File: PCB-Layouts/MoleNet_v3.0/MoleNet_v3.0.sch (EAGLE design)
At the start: 58 parts, among them Q3 BS250, Q4 BS170, Q5 BS250, Q6 BS170, Q7 BS250, Q8 BS170, U1 MCP1703DB, U2 ATMEGA1284p, U4 25LC080P, U5 MCP7940M, U7 BATHOLDER, X1 SMA-142-0711-821/826

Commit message: Updated schematic and board file v3.0
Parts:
- removed JP10, JP12: (no value), pinhead:PINHD-1X12
- removed R13: 4.7K, rcl:R-EU_0207/10
- added JP7: (no value), pinhead:PINHD-1X13
- added JP8: (no value), pinhead:PINHD-1X11
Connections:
- removed net PCINT23: JP12.3, U2.TOSC2/PCINT23
- removed net VSEN+: JP6.2
- net +3V3: no longer R13.2
- net ADC1: now also JP7.1; no longer R13.1
- net ADC2: now also JP7.9; no longer JP10.8
- net ADC3: now also JP7.12; no longer JP10.11
- net ADC4: now also JP7.13; no longer JP10.12
- net ADC5: now also JP7.8; no longer JP10.7
- net ADC6: now also JP7.5; no longer JP10.4
- net ADC7: now also JP7.4; no longer JP10.3
- net ADCVCC: now also JP7.11, JP7.3, JP7.7; no longer JP10.10, JP10.2, JP10.6
- net DIGVCC: now also JP8.2, JP8.5, JP8.9; no longer JP12.10, JP12.2, JP12.6
- net GND: now also JP6.2, JP7.10, JP7.2, JP7.6, JP8.1, JP8.4, JP8.8; no longer JP10.1, JP10.5, JP10.9, JP12.1, JP12.5, JP12.9
- net NSS: now also U2.TOSC2/PCINT23
- net PCINT18: now also JP8.11; no longer JP12.12
- net PCINT19: now also JP8.10; no longer JP12.11
- net PCINT20: now also JP8.7; no longer JP12.8
- net PCINT21: now also JP8.6; no longer JP12.7
- net PCINT22: now also JP8.3; no longer JP12.4

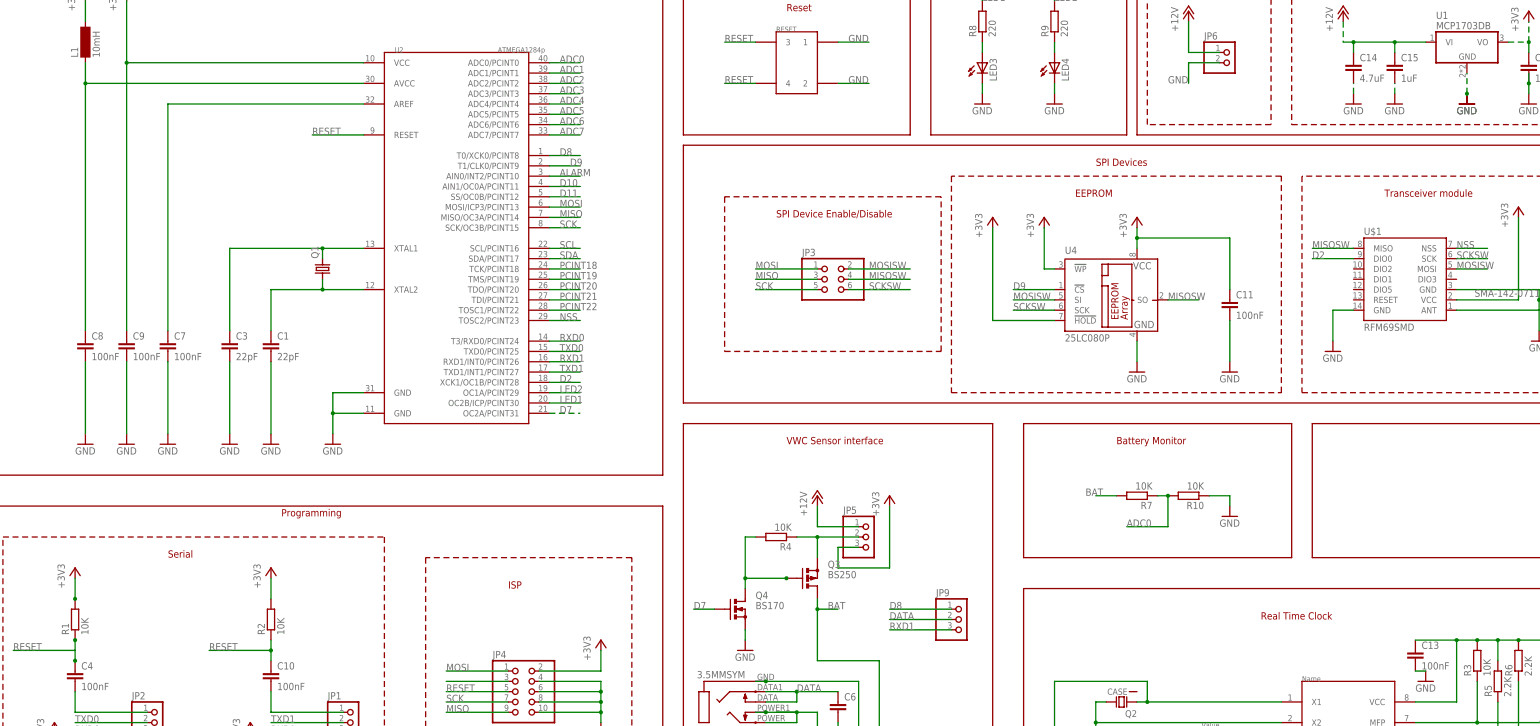
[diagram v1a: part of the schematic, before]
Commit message: redundant files removed
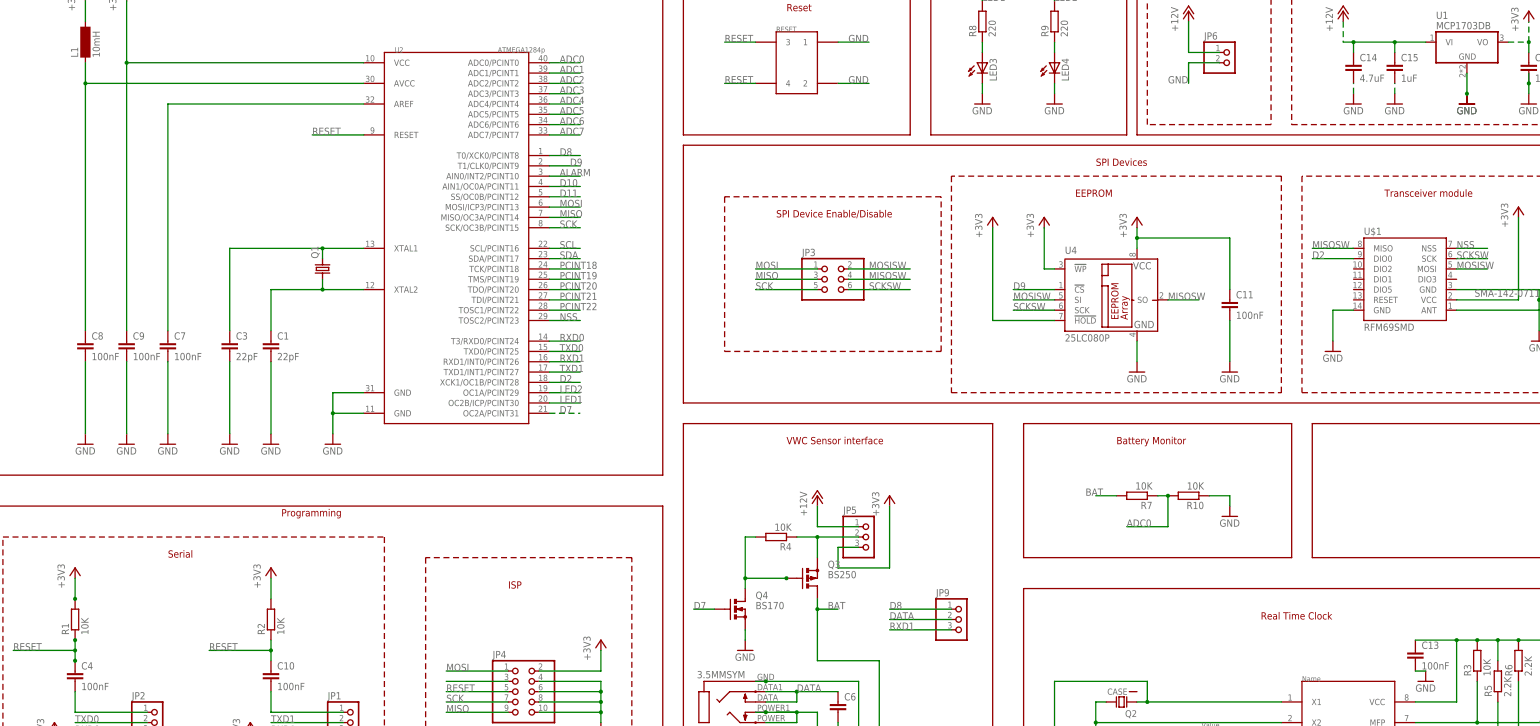
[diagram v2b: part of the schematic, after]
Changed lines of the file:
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@@
 <segment>
 <pinref part="GND19" gate="1" pin="GND"/>
+<pinref part="GND21" gate="1" pin="GND"/>
 <pinref part="U1" gate="G$1" pin="GND"/>
-<wire x1="261.62" y1="129.54" x2="261.62" y2="134.62" width="0.1524" layer="91" style="longdash"/>
-<pinref part="GND21" gate="1" pin="GND"/>
+<wire x1="261.62" y1="129.54" x2="261.62" y2="134.62" width="0.1524" layer="91"/>
 <junction x="261.62" y="129.54"/>
 </segment>
@@
 <wire x1="-81.28" y1="-7.62" x2="-81.28" y2="-5.08" width="0.1524" layer="91"/>
 <wire x1="-96.52" y1="-7.62" x2="-81.28" y2="-7.62" width="0.1524" layer="91"/>
+<junction x="-81.28" y="-7.62"/>
 </segment>
 <segment>
@@
 </sheet>
 </sheets>
+<errors>
+</errors>
 </schematic>
 </drawing>
